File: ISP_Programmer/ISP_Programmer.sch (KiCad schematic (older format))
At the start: 18 parts, among them IC1 ATTINY2313-S, P1 CONN_02X03, P2 USB_OTG, U2 74LS125, X1 CRYSTAL_SMD

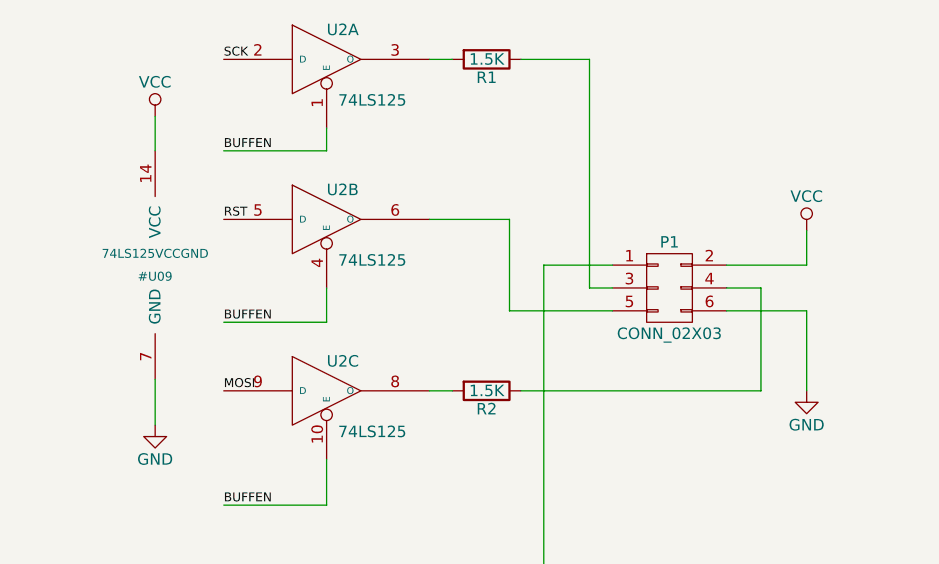
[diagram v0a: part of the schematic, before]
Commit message: ISP footprints
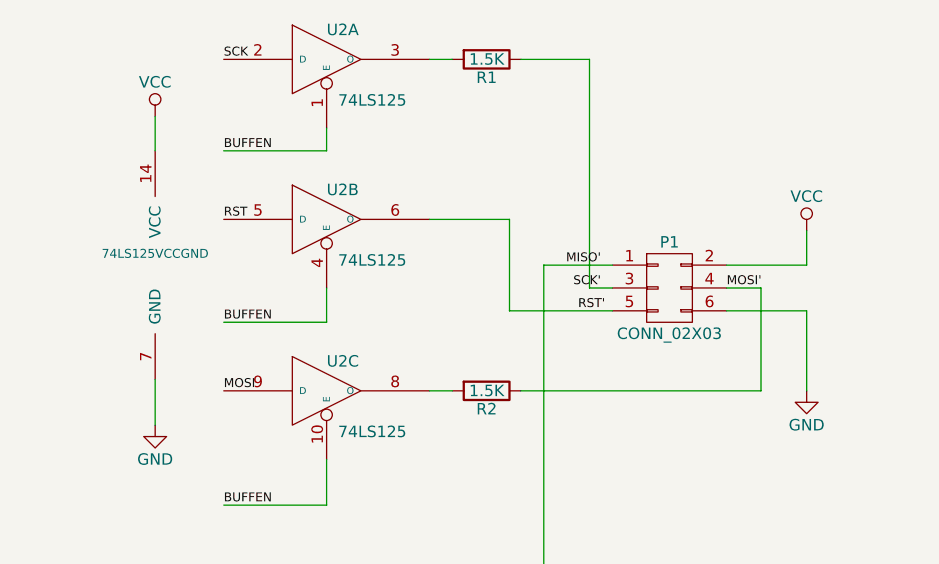
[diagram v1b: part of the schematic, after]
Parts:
- IC1: footprint (none) -> DM_Custom:DM_ATTINY2313_20S2
- P2: footprint (none) -> Connect:USB_Micro-B
- U2: footprint (none) -> DM_Custom:DM_SOP14
- X1: footprint (none) -> DM_Custom:DM_PBRC-H
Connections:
- net RST': now reaches P1.5 (P5), U2.6 (O)
- net MISO': now reaches P1.1 (P1), U2.12 (D)
- net SCK': now reaches P1.3 (P3), R1.1
- net MOSI': now reaches P1.4 (P4), R2.1
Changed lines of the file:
@@
 LIBS:valves
 LIBS:DM_Custom
+LIBS:ISP_Programmer-cache
 EELAYER 25 0
 EELAYER END
@@
 F 0 "IC1" H 1950 6400 50  0000 C CNN
 F 1 "ATTINY2313-S" H 3650 4500 50  0000 C CNN
-F 2 "" H 2900 5400 50  0001 C CIN
+F 2 "DM_Custom:DM_ATTINY2313_20S2" H 2900 5400 50  0001 C CIN
 F 3 "" H 2900 5400 50  0000 C CNN
 	1    2900 5400
@@
 F 0 "U2" H 2250 1200 50  0000 L BNN
 F 1 "74LS125" H 2300 950 50  0000 L TNN
-F 2 "" H 2250 1100 50  0001 C CNN
+F 2 "DM_Custom:DM_SOP14" H 2250 1100 50  0001 C CNN
 F 3 "" H 2250 1100 50  0000 C CNN
 	1    2250 1100
@@
 F 0 "U2" H 2250 1900 50  0000 L BNN
 F 1 "74LS125" H 2300 1650 50  0000 L TNN
-F 2 "" H 2250 1800 50  0001 C CNN
+F 2 "DM_Custom:DM_SOP14" H 2250 1800 50  0001 C CNN
 F 3 "" H 2250 1800 50  0000 C CNN
 	2    2250 1800
@@
 F 0 "U2" H 2250 2650 50  0000 L BNN
 F 1 "74LS125" H 2300 2400 50  0000 L TNN
-F 2 "" H 2250 2550 50  0001 C CNN
+F 2 "DM_Custom:DM_SOP14" H 2250 2550 50  0001 C CNN
 F 3 "" H 2250 2550 50  0000 C CNN
 	3    2250 2550
@@
 F 0 "U2" H 3950 3650 50  0000 L BNN
 F 1 "74LS125" H 4000 3400 50  0000 L TNN
-F 2 "" H 3950 3550 50  0001 C CNN
+F 2 "DM_Custom:DM_SOP14" H 3950 3550 50  0001 C CNN
 F 3 "" H 3950 3550 50  0000 C CNN
 	4    3950 3550
@@
 F 0 "X1" H 1250 5140 50  0000 C CNN
 F 1 "CRYSTAL_SMD" H 1280 4940 50  0000 L CNN
-F 2 "" H 1250 5050 50  0001 C CNN
+F 2 "DM_Custom:DM_PBRC-H" H 1250 5050 50  0001 C CNN
 F 3 "" H 1250 5050 50  0000 C CNN
 	1    1250 5050
@@
 F 0 "P2" H 6125 5575 50  0000 C CNN
 F 1 "USB_OTG" H 5800 5900 50  0000 C CNN
-F 2 "" V 5750 5600 50  0001 C CNN
+F 2 "Connect:USB_Micro-B" V 5750 5600 50  0001 C CNN
 F 3 "" V 5750 5600 50  0000 C CNN
 	1    5800 5700
@@
 U 1 1 592454BB
 P 1500 1950
-F 0 "#U09" H 1500 1850 39  0000 C CNN
+F 0 "#U09" H 1500 1850 39  0001 C CNN
 F 1 "74LS125VCCGND" H 1500 1950 39  0000 C CNN
 F 2 "" H 1500 1950 39  0001 C CNN
@@
 NoConn ~ 4050 4800
 NoConn ~ 4050 4900
+Text Label 4000 2100 0    39   ~ 0
+MOSI'
+Text Label 3450 2000 2    39   ~ 0
+MISO'
+Text Label 3350 2200 0    39   ~ 0
+RST'
+Text Label 3450 2100 2    39   ~ 0
+SCK'
 $EndSCHEMATC
